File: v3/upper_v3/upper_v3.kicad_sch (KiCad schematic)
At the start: 3 parts, among them J1 Conn_01x18, J2 Conn_01x09_Male, J3 Conn_01x09_Male

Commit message: Complete Toast PCB
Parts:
- removed J1: Conn_01x18, Connector_PinHeader_2.54mm:PinHeader_1x18_P2.54mm_Horizontal, symbol Connector_Generic:Conn_01x18
- removed J2, J3: Conn_01x09_Male, Connector_PinSocket_2.54mm:PinSocket_1x09_P2.54mm_Vertical, symbol Connector:Conn_01x09_Male
- added J1: Conn_01x24, Connector_PinHeader_2.54mm:PinHeader_1x24_P2.54mm_Horizontal, symbol Connector_Generic:Conn_01x24
- added J2, J3: Conn_01x05_Female, Connector_PinSocket_2.54mm:PinSocket_1x05_P2.54mm_Vertical, symbol Connector:Conn_01x05_Female
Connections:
- new net: J1.23 (Pin_23), J2.1 (Pin_1)
- new net: J1.20 (Pin_20), J2.2 (Pin_2)
- new net: J1.17 (Pin_17), J2.3 (Pin_3)
- new net: J1.14 (Pin_14), J2.4 (Pin_4)
- new net: J1.1 (Pin_1), J1.10 (Pin_10), J1.13 (Pin_13), J1.16 (Pin_16), J1.19 (Pin_19), J1.22 (Pin_22), J1.4 (Pin_4), J1.7 (Pin_7), J2.5 (Pin_5)
- new net: J1.11 (Pin_11), J3.2 (Pin_2)
- new net: J1.12 (Pin_12), J1.15 (Pin_15), J1.18 (Pin_18), J1.21 (Pin_21), J1.24 (Pin_24), J1.3 (Pin_3), J1.6 (Pin_6), J1.9 (Pin_9), J3.1 (Pin_1)
- new net: J1.2 (Pin_2), J3.5 (Pin_5)
- new net: J1.5 (Pin_5), J3.4 (Pin_4)
- new net: J1.8 (Pin_8), J3.3 (Pin_3)
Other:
- note added: "Ground"
- note added: "VDD-3V"

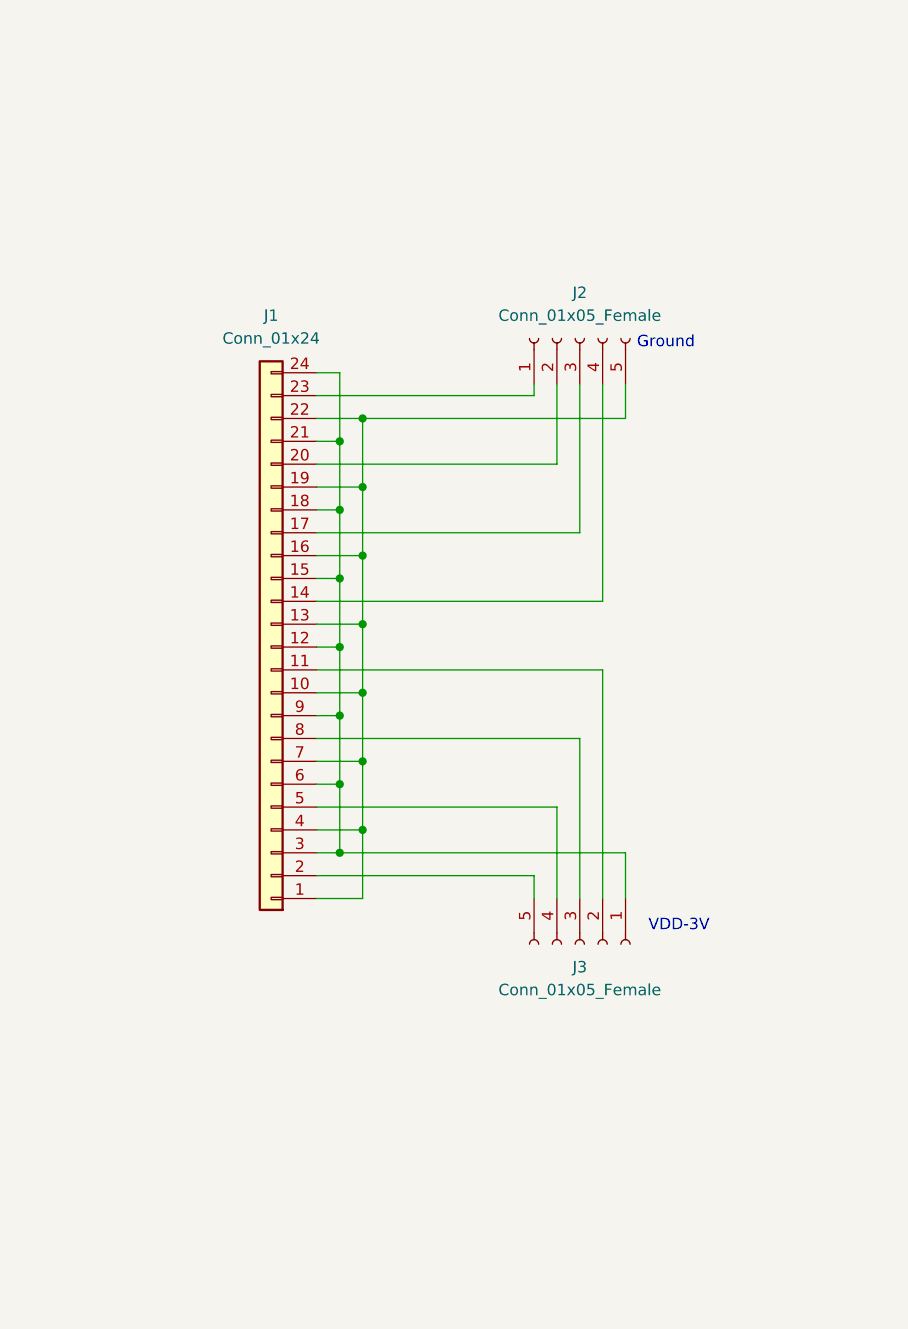
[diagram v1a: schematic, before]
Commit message: Rev.A Toast Design, fixing connection between 2 boards, adding 3 I/O for the DOME, creating blank proto area for testing
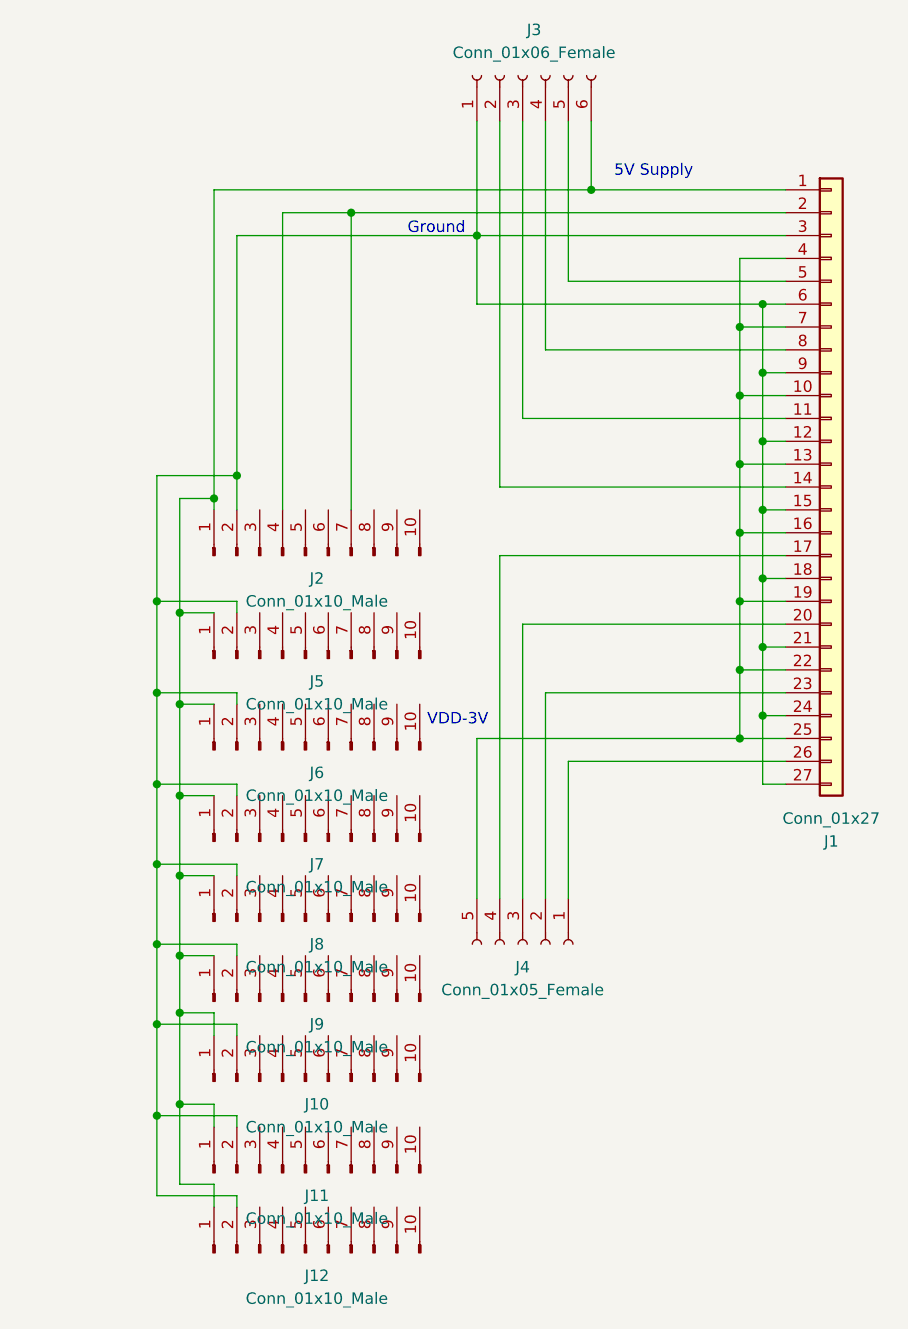
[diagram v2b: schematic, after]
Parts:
- removed J1: Conn_01x24, Connector_PinHeader_2.54mm:PinHeader_1x24_P2.54mm_Horizontal, symbol Connector_Generic:Conn_01x24
- removed J2, J3: Conn_01x05_Female, Connector_PinSocket_2.54mm:PinSocket_1x05_P2.54mm_Vertical, symbol Connector:Conn_01x05_Female
- added J1: Conn_01x27, Connector_PinHeader_2.54mm:PinHeader_1x27_P2.54mm_Horizontal, symbol Connector_Generic:Conn_01x27
- added J10, J11, J12, J2, J5, J6, J7, J8, J9: Conn_01x10_Male, Connector_PinHeader_2.54mm:PinHeader_1x10_P2.54mm_Vertical, symbol Connector:Conn_01x10_Male
- added J3: Conn_01x06_Female, Connector_PinSocket_2.54mm:PinSocket_1x06_P2.54mm_Vertical, symbol Connector:Conn_01x06_Female
- added J4: Conn_01x05_Female, Connector_PinSocket_2.54mm:PinSocket_1x05_P2.54mm_Vertical, symbol Connector:Conn_01x05_Female
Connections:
- new net: J1.1 (Pin_1), J10.1 (Pin_1), J11.1 (Pin_1), J12.1 (Pin_1), J2.1 (Pin_1), J3.6 (Pin_6), J5.1 (Pin_1), J6.1 (Pin_1), J7.1 (Pin_1), J8.1 (Pin_1), J9.1 (Pin_1)
- new net: J1.12 (Pin_12), J1.15 (Pin_15), J1.18 (Pin_18), J1.21 (Pin_21), J1.24 (Pin_24), J1.27 (Pin_27), J1.3 (Pin_3), J1.6 (Pin_6), J1.9 (Pin_9), J10.2 (Pin_2), J11.2 (Pin_2), J12.2 (Pin_2), J2.2 (Pin_2), J3.1 (Pin_1), J5.2 (Pin_2), J6.2 (Pin_2), J7.2 (Pin_2), J8.2 (Pin_2), J9.2 (Pin_2)
- new net: J1.14 (Pin_14), J3.2 (Pin_2)
- new net: J1.11 (Pin_11), J3.3 (Pin_3)
- new net: J1.8 (Pin_8), J3.4 (Pin_4)
- new net: J1.5 (Pin_5), J3.5 (Pin_5)
- new net: J1.10 (Pin_10), J1.13 (Pin_13), J1.16 (Pin_16), J1.19 (Pin_19), J1.22 (Pin_22), J1.25 (Pin_25), J1.4 (Pin_4), J1.7 (Pin_7), J4.5 (Pin_5)
- new net: J1.17 (Pin_17), J4.4 (Pin_4)
- new net: J1.2 (Pin_2), J2.4 (Pin_4), J2.7 (Pin_7)
- new net: J1.20 (Pin_20), J4.3 (Pin_3)
- new net: J1.23 (Pin_23), J4.2 (Pin_2)
- new net: J1.26 (Pin_26), J4.1 (Pin_1)
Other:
- note added: "5V Supply"

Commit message: Add pin detail, fixing layout annotation on board
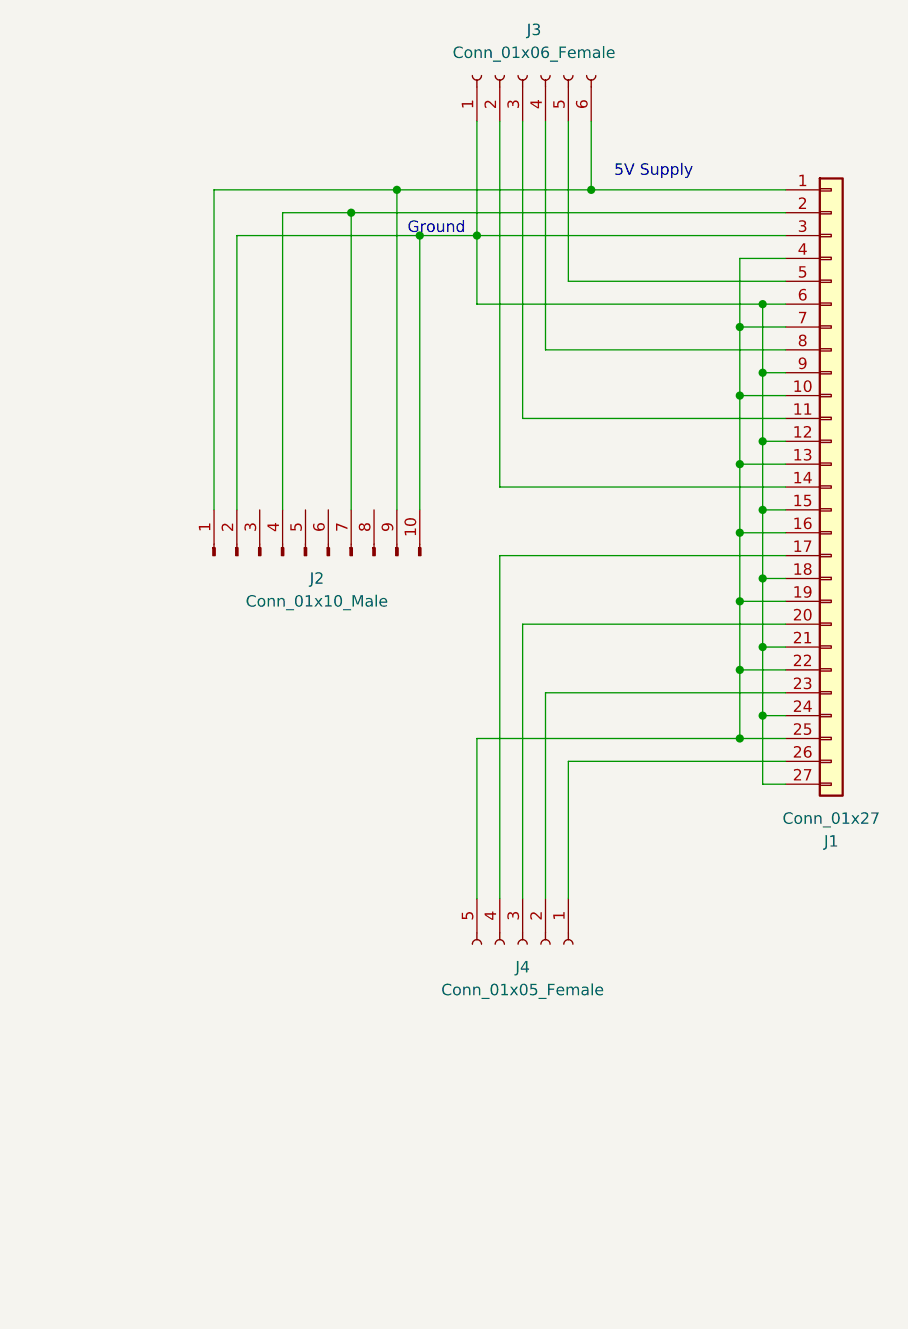
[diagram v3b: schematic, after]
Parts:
- removed J10, J11, J12, J5, J6, J7, J8, J9: Conn_01x10_Male, Connector_PinHeader_2.54mm:PinHeader_1x10_P2.54mm_Vertical, symbol Connector:Conn_01x10_Male
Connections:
- net at J1.1 (Pin_1), J2.1 (Pin_1), J3.6 (Pin_6): now also J2.9 (Pin_9)
- net at J1.12 (Pin_12), J1.15 (Pin_15), J1.18 (Pin_18)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: now also J2.10 (Pin_10)
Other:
- note removed: "VDD-3V"
